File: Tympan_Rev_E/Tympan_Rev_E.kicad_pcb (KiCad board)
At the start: 4 copper layers, 38 x 74 mm, 98 parts, among them IC1 BC127-EXT, J1 SJ-3523-SMT-TR, J2 SJ-3524-SMT-TR-PI, J3 Opt Breakout, J4 Qwiik Connector, J5 SMT, J6 SMT, P1 CONN_01X06, P2 CONN_01X06, P3 CONN_01X06, P4 CONN_01X06, P6 CONN_01X01, P7 CONN_01X01, P8 CONN_01X01, SW1 CL-SB-22A, SW2 SW_Push, U1 MCP73831, U2 TLV320AIC3206IRSBT, U3 74LVC1G66, U4 MIC5323-1.8YD5-TR, U5 Teensy4.1, U6 LC709203

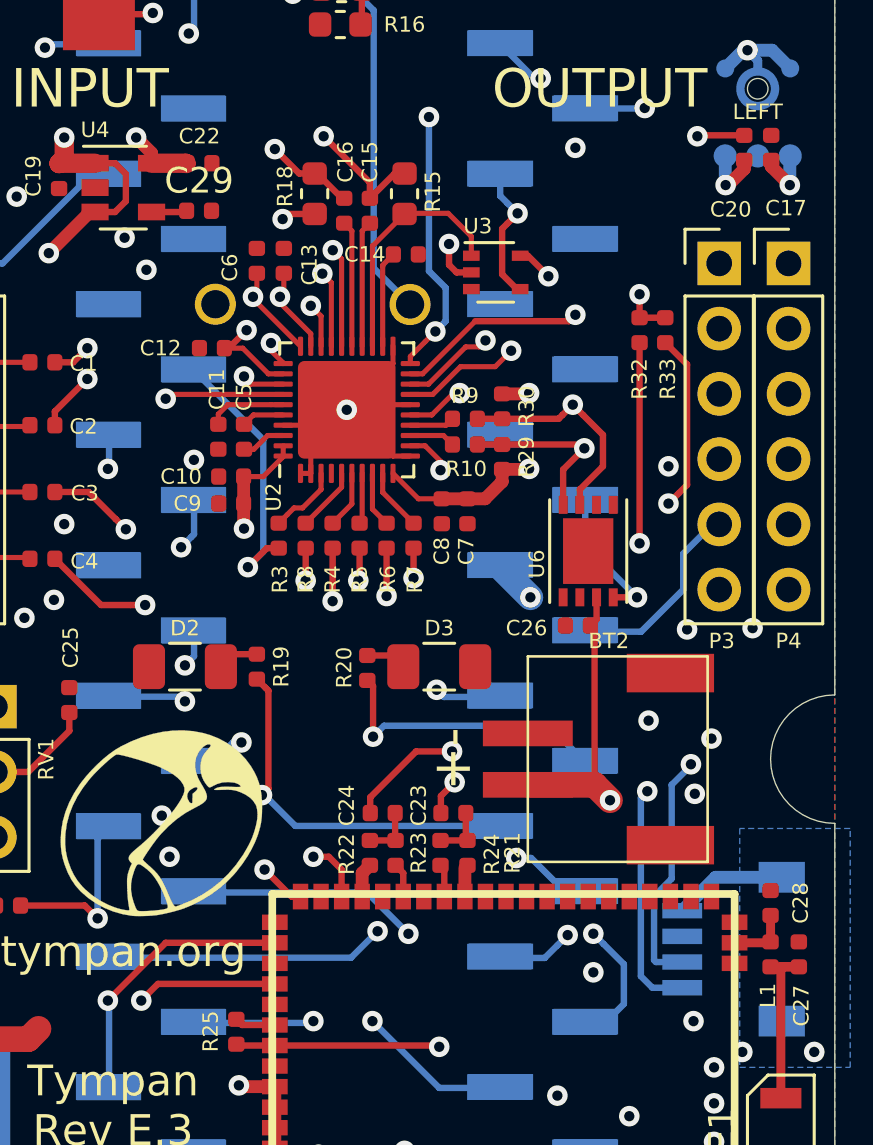
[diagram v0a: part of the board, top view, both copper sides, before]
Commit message: Working out supply chain kinks and polishing this version
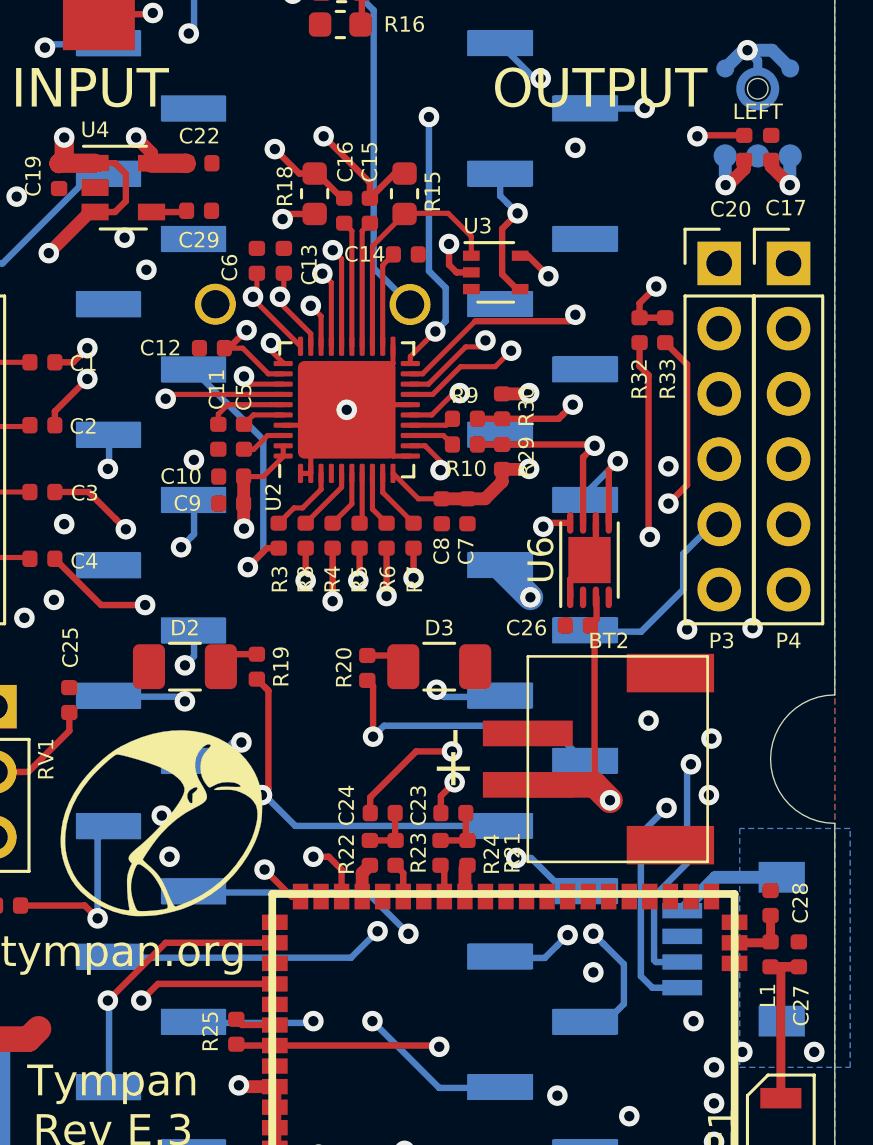
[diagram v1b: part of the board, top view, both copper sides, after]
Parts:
- D2: value LED -> RED_LED
- D3: value LED -> GREEN_LED
- U6: value LC709203 -> MAX7148; footprint Tympan:WDFN8_3X4mm_0.65P -> Package_DFN_QFN:TDFN-8-1EP_3x2mm_P0.5mm_EP1.80x1.65mm
- moved U6 0.35 mm to (162.8, 96.0), turned to 90 degrees
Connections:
- BT2 pad 3: GND -> (no net)
- BT2 pad 4: GND -> (no net)
- J4 pad : GND -> (no net)
- U6 pad 2: GND -> Net-(U6-Pad2)
- U6 pad 4: /ALARMB -> GND
- U6 pad 5: Net-(U6-Pad5) -> /ALARMB
- U6 pad 6: Net-(U6-Pad6) -> GND
- U6 pad 7: /SDA -> /SCL
- U6 pad 8: /SCL -> /SDA
- U6 pad 9: GND -> (no net)
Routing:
- net GND: track 82.2 -> 85.5 mm
- net /SDA: track 32.6 -> 29.6 mm, vias 2 -> 3
- net /SCL: track 30.9 -> 32.1 mm
- net /34_RX8: track 78.1 -> 79.1 mm
- net /ALARMB: track 5.50 -> 4.63 mm
- net +3V3: track 28.6 -> 29.2 mm
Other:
- board text added: "This Branch Uses BC127-EXT Module Variants"
- board text removed: "This Branch Uses BC127-EXT Module Variant"

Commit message: Freezing. In Production
Project is on Circuit Hub in Revision 8
https://circuithub.com/projects/biomurph/Tympan_Rev_E/revisions/40091/viewer
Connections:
- J4 pad : (no net) -> GND
- U6 pad 9: (no net) -> GND
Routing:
- net Net-(F1-Pad1): track 27.7 -> 24.9 mm
- net /R: track 21.5 -> 19.0 mm, vias 1 -> 0
- net /L: track 9.26 -> 8.23 mm, vias 1 -> 0

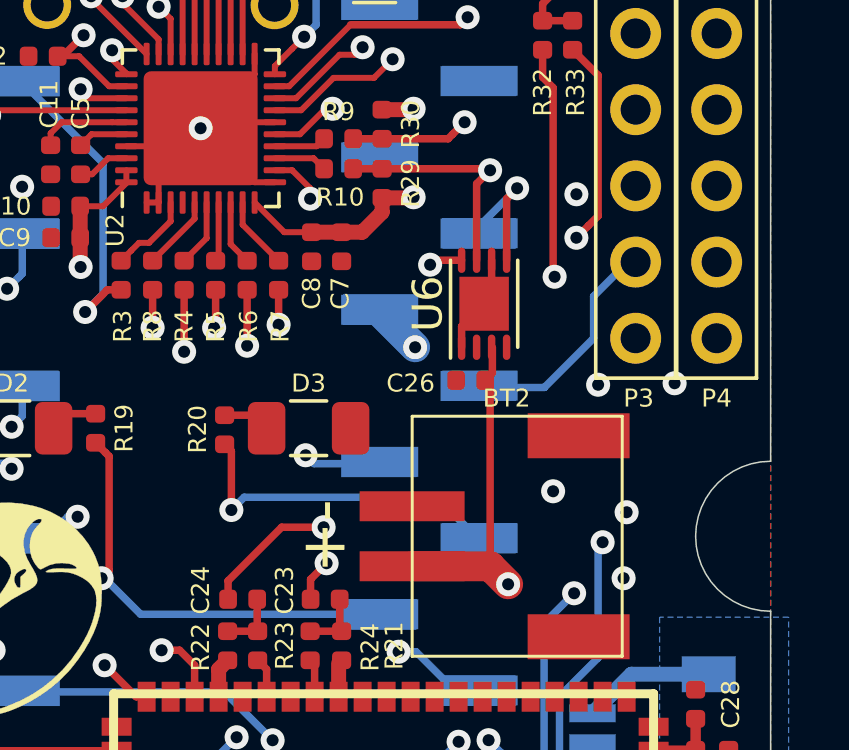
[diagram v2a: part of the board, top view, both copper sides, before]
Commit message: Production Update
Change U6 footprint to match package
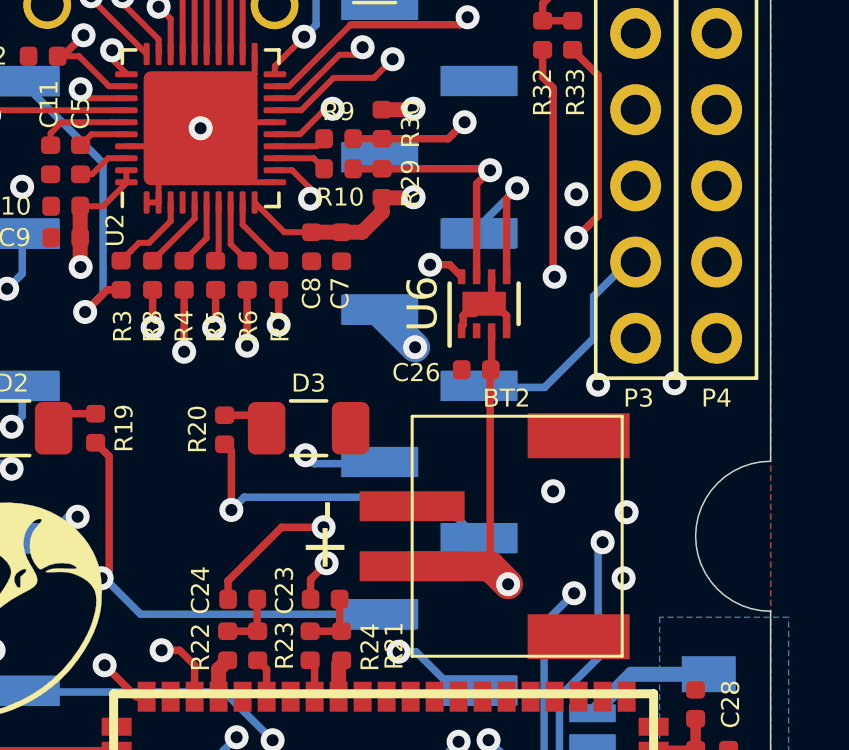
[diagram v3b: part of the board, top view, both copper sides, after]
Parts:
- C26: value 1uF -> 0.1uF
- U6: value MAX7148 -> MAX17048; footprint Package_DFN_QFN:TDFN-8-1EP_3x2mm_P0.5mm_EP1.80x1.65mm -> Tympan:TDFN-8-1EP_2x2mm_Pitch0.5mm
- moved C26 0.40 mm to (162.6, 98.2)
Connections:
- BT2 pad 3: (no net) -> GND
- BT2 pad 4: (no net) -> GND
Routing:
- net /SCL: track 32.1 -> 32.7 mm
- net /ALARMB: track 4.63 -> 5.18 mm
